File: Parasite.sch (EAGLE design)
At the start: 22 parts, among them U1 ATMEGA328PB-AU, U2 AD5262AD5262, U3 AD5262AD5262, U4 AD5262AD5262

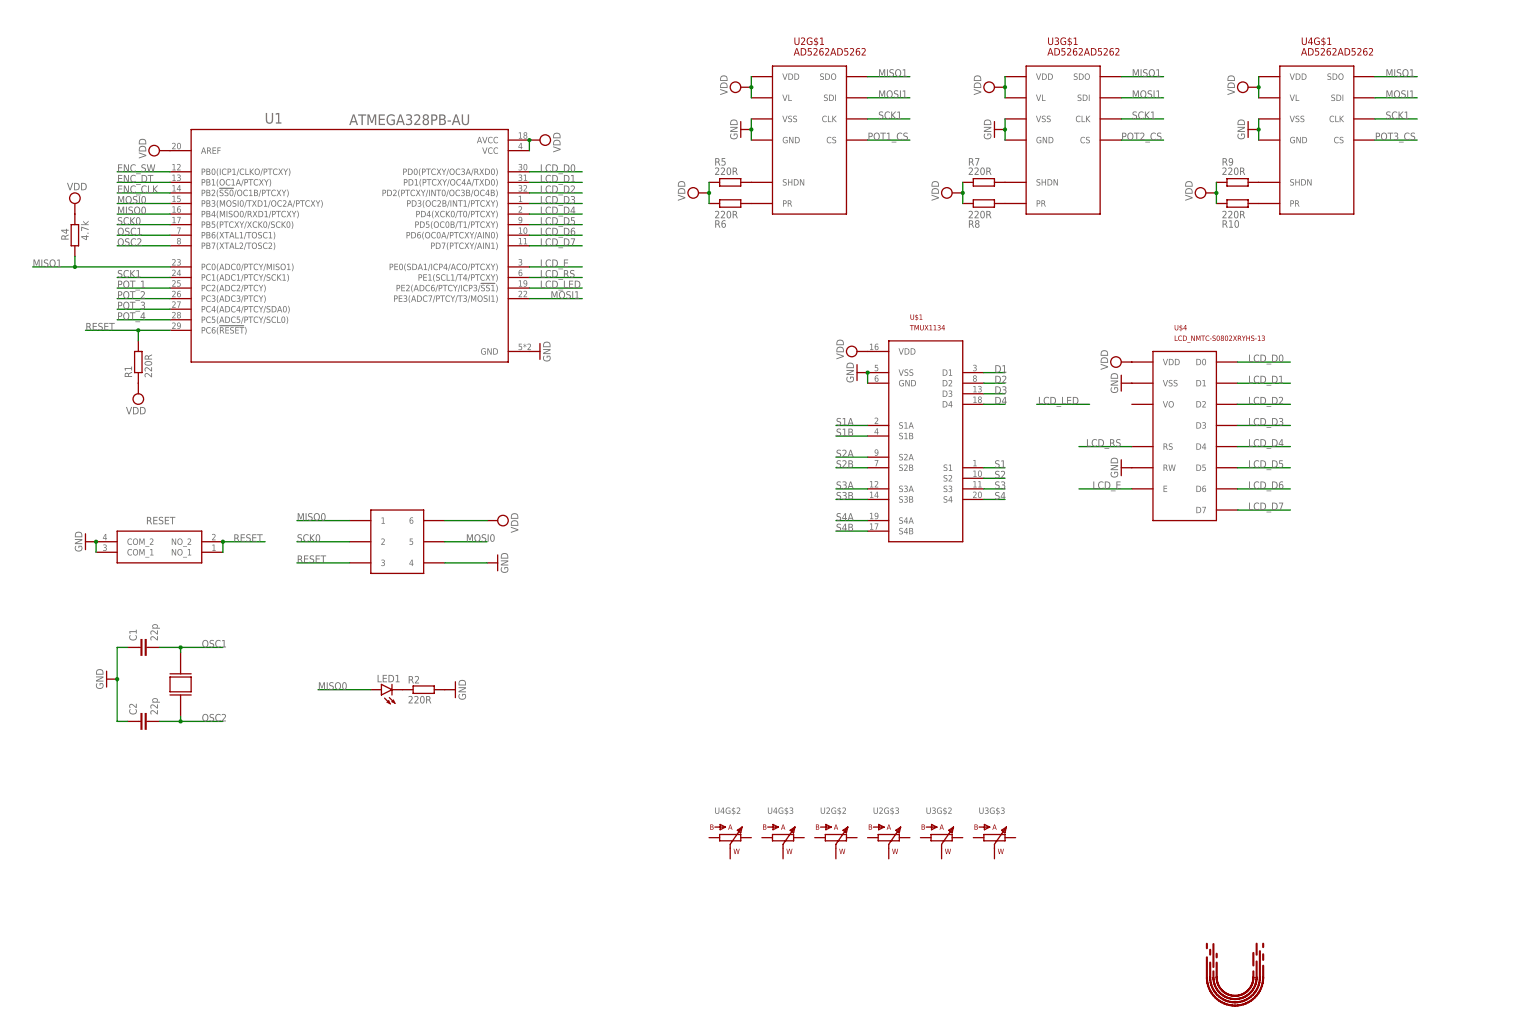
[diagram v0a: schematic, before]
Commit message: Added components and initialized layout
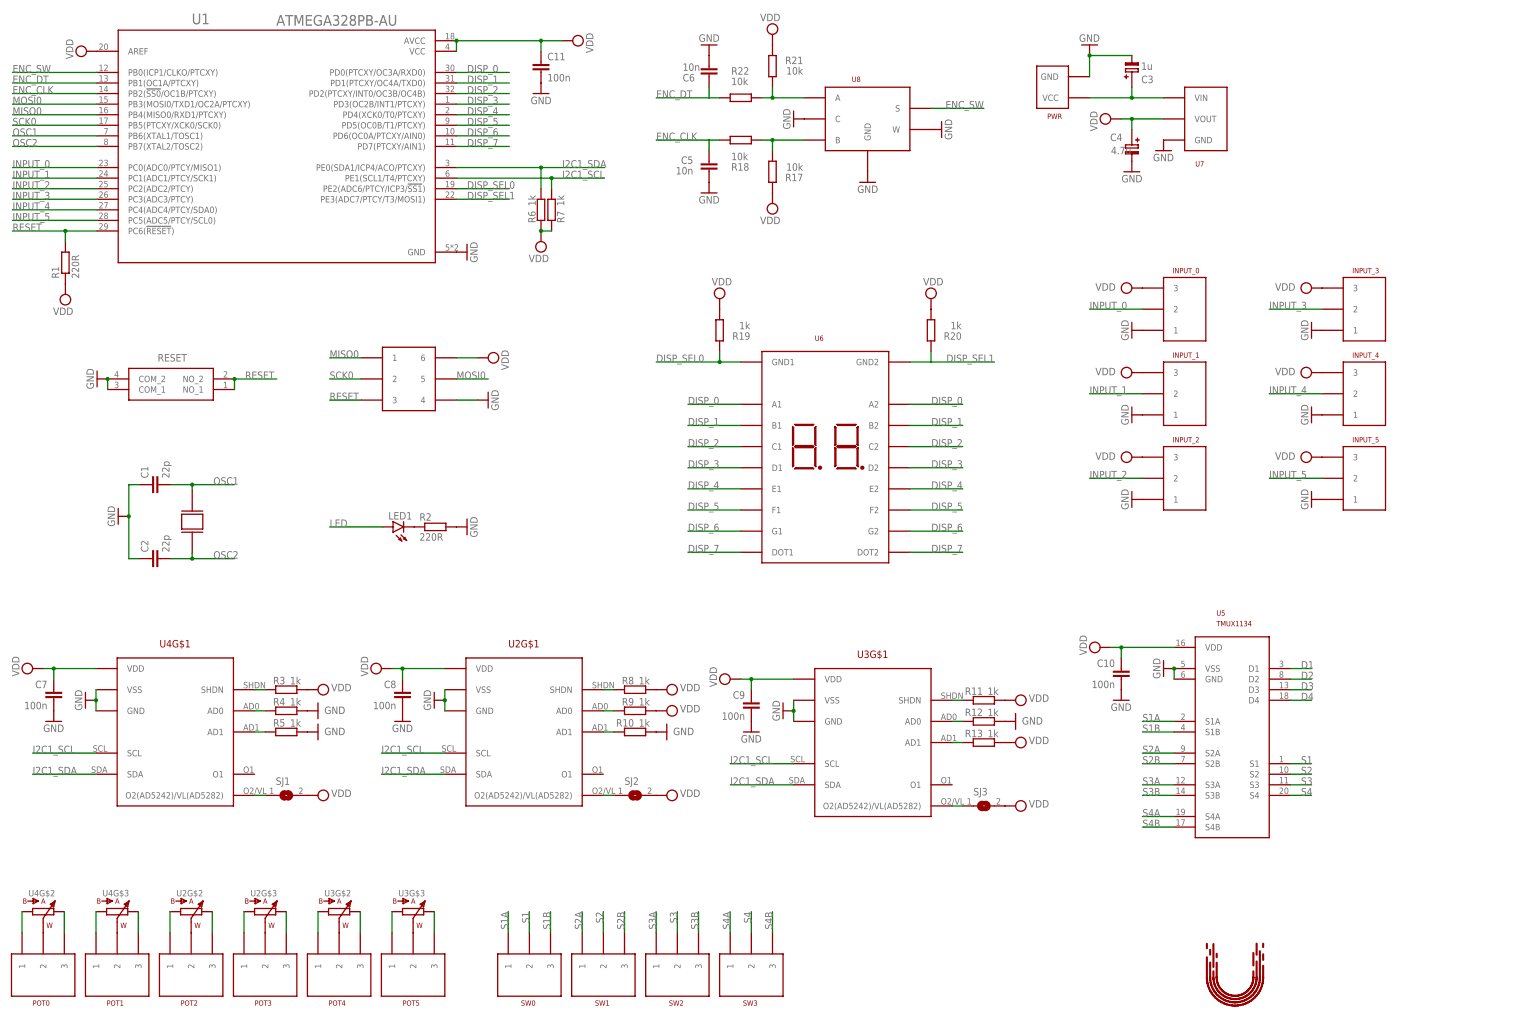
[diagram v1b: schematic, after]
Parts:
- removed U$1: TMUX1134, lib:TMUX1134
- removed U$4: LCD_NMTC-S0802XRYHS-13, lib:LCD_NMTC-S0802XRYHS-13
- added C10, C11, C7, C8, C9: 100n, lib:CAPACITOR1206
- added C3: 1u, lib:ELECT_CAPACITORCAP6
- added C4: 4.7u, lib:ELECT_CAPACITORCAP6
- added C5, C6: 10n, lib:CAPACITOR1206
- added INPUT_0, INPUT_1, INPUT_2, INPUT_3, INPUT_4, INPUT_5, POT0, POT1, POT2, POT3, POT4, POT5, SW0, SW1, SW2, SW3: 3_PIN_CONNECTOR, lib:3_PIN_CONNECTOR
- added PWR: PWR, lib:PWR
- added R11, R12, R13, R19, R20, R3: 1k, lib:RESISTOR1206
- added R17, R18, R21, R22: 10k, lib:RESISTOR1206
- added SJ1, SJ2, SJ3: (no value), lib:JUMPER
- added U5: TMUX1134, lib:TMUX1134
- added U6: 7_SEGMENT_DISPLAY, lib:7_SEGMENT_DISPLAY
- added U7: VOLTAGE_REGULATOR_LDL1117S50RVOLTAGE_REGULATOR_LDL1117S50R, lib:VOLTAGE_REGULATOR_LDL1117S50RVOLTAGE_REGULATOR_LDL1117S50R
- added U8: ROTARY_ENCODER, lib:ROTARY_ENCODER
- LED1: value LEDLED_1206 -> LEDLED_THROUGH; device lib:LEDLED_1206 -> lib:LEDLED_THROUGH
- R10, R5, R6, R7, R8, R9: value 220R -> 1k
- R4: value 4.7k -> 1k
- U2, U4: value AD5262AD5262 -> DIGITAL_POT_AD5242AD5242/AD5282; device lib:AD5262AD5262 -> lib:DIGITAL_POT_AD5242AD5242/AD5282
- U3: value AD5262AD5262 -> DIGITAL_POT_AD5282AD5242/AD5282; device lib:AD5262AD5262 -> lib:DIGITAL_POT_AD5282AD5242/AD5282
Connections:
- removed net LCD_D0: U$4.D0, U1.PD0(PTCXY/OC3A/RXD0)
- removed net LCD_D1: U$4.D1, U1.PD1(PTCXY/OC4A/TXD0)
- removed net LCD_D2: U$4.D2, U1.PD2(PTCXY/INT0/OC3B/OC4B)
- removed net LCD_D3: U$4.D3, U1.PD3(OC2B/INT1/PTCXY)
- removed net LCD_D4: U$4.D4, U1.PD4(XCK0/T0/PTCXY)
- removed net LCD_D5: U$4.D5, U1.PD5(OC0B/T1/PTCXY)
- removed net LCD_D6: U$4.D6, U1.PD6(OC0A/PTCXY/AIN0)
- removed net LCD_D7: U$4.D7, U1.PD7(PTCXY/AIN1)
- removed net LCD_E: U$4.E, U1.PE0(SDA1/ICP4/ACO/PTCXY)
- removed net LCD_LED: U1.PE2(ADC6/PTCY/ICP3/!SS1!)
- removed net LCD_RS: U$4.RS, U1.PE1(SCL1/T4/PTCXY)
- removed net MISO1: R4.1, U1.PC0(ADC0/PTCY/MISO1), U2G$1.SDO, U3G$1.SDO, U4G$1.SDO
- removed net MOSI1: U1.PE3(ADC7/PTCY/T3/MOSI1), U2G$1.SDI, U3G$1.SDI, U4G$1.SDI
- removed net POT1_CS: U2G$1.CS
- removed net POT2_CS: U3G$1.CS
- removed net POT3_CS: U4G$1.CS
- removed net POT_1: U1.PC2(ADC2/PTCY)
- removed net POT_2: U1.PC3(ADC3/PTCY)
- removed net POT_3: U1.PC4(ADC4/PTCY/SDA0)
- removed net POT_4: U1.PC5(ADC5/PTCY/SCL0)
- removed net SCK1: U1.PC1(ADC1/PTCY/SCK1), U2G$1.CLK, U3G$1.CLK, U4G$1.CLK
- new net DISP_0: U1.PD0(PTCXY/OC3A/RXD0), U6.A1, U6.A2
- new net DISP_1: U1.PD1(PTCXY/OC4A/TXD0), U6.B1, U6.B2
- new net DISP_2: U1.PD2(PTCXY/INT0/OC3B/OC4B), U6.C1, U6.C2
- new net DISP_3: U1.PD3(OC2B/INT1/PTCXY), U6.D1, U6.D2
- new net DISP_4: U1.PD4(XCK0/T0/PTCXY), U6.E1, U6.E2
- new net DISP_5: U1.PD5(OC0B/T1/PTCXY), U6.F1, U6.F2
- new net DISP_6: U1.PD6(OC0A/PTCXY/AIN0), U6.G1, U6.G2
- new net DISP_7: U1.PD7(PTCXY/AIN1), U6.DOT1, U6.DOT2
- new net DISP_SEL0: R19.1, U1.PE2(ADC6/PTCY/ICP3/!SS1!), U6.GND1
- new net DISP_SEL1: U1.PE3(ADC7/PTCY/T3/MOSI1), U6.GND2
- new net DISP_SEL2: R20.1
- new net I2C1_SCL: R7.1, U1.PE1(SCL1/T4/PTCXY), U2G$1.SCL, U3G$1.SCL, U4G$1.SCL
- new net I2C1_SDA: R6.1, U1.PE0(SDA1/ICP4/ACO/PTCXY), U2G$1.SDA, U3G$1.SDA, U4G$1.SDA
- new net INPUT_0: INPUT_0.2, U1.PC0(ADC0/PTCY/MISO1)
- new net INPUT_1: INPUT_1.2, U1.PC1(ADC1/PTCY/SCK1)
- new net INPUT_2: INPUT_2.2, U1.PC2(ADC2/PTCY)
- new net INPUT_3: INPUT_3.2, U1.PC3(ADC3/PTCY)
- new net INPUT_4: INPUT_4.2, U1.PC4(ADC4/PTCY/SDA0)
- new net INPUT_5: INPUT_5.2, U1.PC5(ADC5/PTCY/SCL0)
- new net LED: LED1.A
- new net N$10: SJ2.1, U2G$1.O2(AD5242)/VL(AD5282)
- new net N$11: R12.2, U3G$1.AD0
- new net N$12: R13.2, U3G$1.AD1
- new net N$13: SJ3.1, U3G$1.O2(AD5242)/VL(AD5282)
- new net N$18: POT0.2, U4G$2.W
- new net N$19: POT0.1, U4G$2.B
- new net N$2: R3.2, U4G$1.SHDN
- new net N$20: POT0.3, U4G$2.A
- new net N$21: POT1.1, U4G$3.B
- new net N$22: POT1.3, U4G$3.A
- new net N$23: POT1.2, U4G$3.W
- new net N$24: POT2.1, U2G$2.B
- new net N$25: POT2.3, U2G$2.A
- new net N$26: POT2.2, U2G$2.W
- new net N$27: POT3.1, U2G$3.B
- new net N$28: POT3.3, U2G$3.A
- new net N$29: POT3.2, U2G$3.W
- new net N$30: POT4.1, U3G$2.B
- new net N$31: POT4.3, U3G$2.A
- new net N$32: POT4.2, U3G$2.W
- new net N$33: POT5.1, U3G$3.B
- new net N$34: POT5.3, U3G$3.A
- new net N$35: POT5.2, U3G$3.W
- new net N$42: C3.+, PWR.VCC, U7.VIN
- new net N$43: R17.2, R18.1, U8.B
- new net N$45: R21.2, R22.1, U8.A
- new net N$9: R10.2, U2G$1.AD1
- net D1: now also U5.D1; no longer U$1.D1
- net D2: now also U5.D2; no longer U$1.D2
- net D3: now also U5.D3; no longer U$1.D3
- net D4: now also U5.D4; no longer U$1.D4
- net ENC_CLK: now also C5.2, R18.2
- net ENC_DT: now also C6.2, R22.2
- net ENC_SW: now also U8.S
- net GND: now also C10.2, C11.2, C3.-, C4.-, C5.1, C6.1, C7.2, C8.2, C9.2, INPUT_0.1, INPUT_1.1, INPUT_2.1, INPUT_3.1, INPUT_4.1, INPUT_5.1, PWR.GND, R10.1, R12.1, R4.1, R5.1, U5.GND, U5.VSS, U7.GND, U8.C, U8.GND, U8.W; no longer U$1.GND, U$1.VSS, U$4.RW, U$4.VSS
- net MISO0: no longer LED1.A
- net N$3: now also R4.2, U4G$1.AD0; no longer R5.2, U2G$1.SHDN
- net N$4: now also R5.2, U4G$1.AD1; no longer R6.2, U2G$1.PR
- net N$5: now also SJ1.1, U4G$1.O2(AD5242)/VL(AD5282); no longer R7.2, U3G$1.SHDN
- net N$6: now also R11.2, U3G$1.SHDN; no longer R8.2, U3G$1.PR
- net N$7: now also R8.2, U2G$1.SHDN; no longer R9.2, U4G$1.SHDN
- net N$8: now also R9.2, U2G$1.AD0; no longer R10.2, U4G$1.PR
- net S1: now also SW0.2, U5.S1; no longer U$1.S1
- net S1A: now also SW0.1, U5.S1A; no longer U$1.S1A
- net S1B: now also SW0.3, U5.S1B; no longer U$1.S1B
- net S2: now also SW1.2, U5.S2; no longer U$1.S2
- net S2A: now also SW1.1, U5.S2A; no longer U$1.S2A
- net S2B: now also SW1.3, U5.S2B; no longer U$1.S2B
- net S3: now also SW2.2, U5.S3; no longer U$1.S3
- net S3A: now also SW2.1, U5.S3A; no longer U$1.S3A
- net S3B: now also SW2.3, U5.S3B; no longer U$1.S3B
- net S4: now also SW3.2, U5.S4; no longer U$1.S4
- net S4A: now also SW3.1, U5.S4A; no longer U$1.S4A
- net S4B: now also SW3.3, U5.S4B; no longer U$1.S4B
- net VDD: now also C10.1, C11.1, C4.+, C7.1, C8.1, C9.1, INPUT_0.3, INPUT_1.3, INPUT_2.3, INPUT_3.3, INPUT_4.3, INPUT_5.3, R11.1, R13.1, R17.1, R19.2, R20.2, R21.1, R3.1, R6.2, R7.2, SJ1.2, SJ2.2, SJ3.2, U5.VDD, U7.VOUT; no longer R10.1, R4.2, R5.1, R6.1, R7.1, U$1.VDD, U$4.VDD, U2G$1.VL, U3G$1.VL, U4G$1.VL
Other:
- moved on the sheet: C1, C2, LED1, R1, R10, R2, R4, R5, R6, R7, R8, R9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

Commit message: Finished v1 layout
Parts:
- renumbered U$2 to U9, U$3 to U10
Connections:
- removed net DISP_SEL2: R20.1
- removed net LED: LED1.A
- removed net MOSI0: U1.PB3(MOSI0/TXD1/OC2A/PTCXY), U9.5
- removed net N$32: POT4.2, U3G$2.W
- removed net N$33: POT5.1, U3G$3.B
- removed net N$34: POT5.3, U3G$3.A
- removed net N$35: POT5.2, U3G$3.W
- new net MOSI0/LED: LED1.A, U1.PB3(MOSI0/TXD1/OC2A/PTCXY), U9.5
- new net N$14: POT2.2, U3G$3.W
- new net N$15: POT1.2, U2G$2.W
- new net N$16: POT0.2, U2G$3.W
- new net N$17: POT4.2, U4G$3.W
- net DISP_2: now also U6.E1, U6.E2; no longer U6.C1, U6.C2
- net DISP_4: now also U6.C1, U6.C2; no longer U6.E1, U6.E2
- net DISP_SEL1: now also R20.1
- net N$18: now also POT5.2; no longer POT0.2
- net N$19: now also POT3.2, U3G$2.W; no longer POT0.1, U4G$2.B
- net N$20: now also U2G$3.A; no longer U4G$2.A
- net N$21: now also POT0.1, U2G$3.B; no longer POT1.1, U4G$3.B
- net N$22: now also POT3.1, U3G$2.B; no longer POT1.3, U4G$3.A
- net N$23: now also POT3.3, U3G$2.A; no longer POT1.2, U4G$3.W
- net N$24: now also U3G$3.B; no longer U2G$2.B
- net N$25: now also U3G$3.A; no longer U2G$2.A
- net N$26: now also POT1.1, U2G$2.B; no longer POT2.2, U2G$2.W
- net N$27: now also POT1.3, U2G$2.A; no longer POT3.1, U2G$3.B
- net N$28: now also POT4.3, U4G$3.A; no longer POT3.3, U2G$3.A
- net N$29: now also POT5.3, U4G$2.A; no longer POT3.2, U2G$3.W
- net N$30: now also U4G$3.B; no longer U3G$2.B
- net N$31: now also POT5.1, U4G$2.B; no longer POT4.3, U3G$2.A
- net S1: now also SW1.2; no longer SW0.2
- net S1A: now also SW1.1; no longer SW0.1
- net S1B: now also SW1.3; no longer SW0.3
- net S2: now also SW0.2; no longer SW1.2
- net S2A: now also SW0.1; no longer SW1.1
- net S2B: now also SW0.3; no longer SW1.3
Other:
- moved on the sheet: SW0, SW1, SW2, SW3, U2G$2, U2G$3, U3G$2, U3G$3, U4G$2, U4G$3

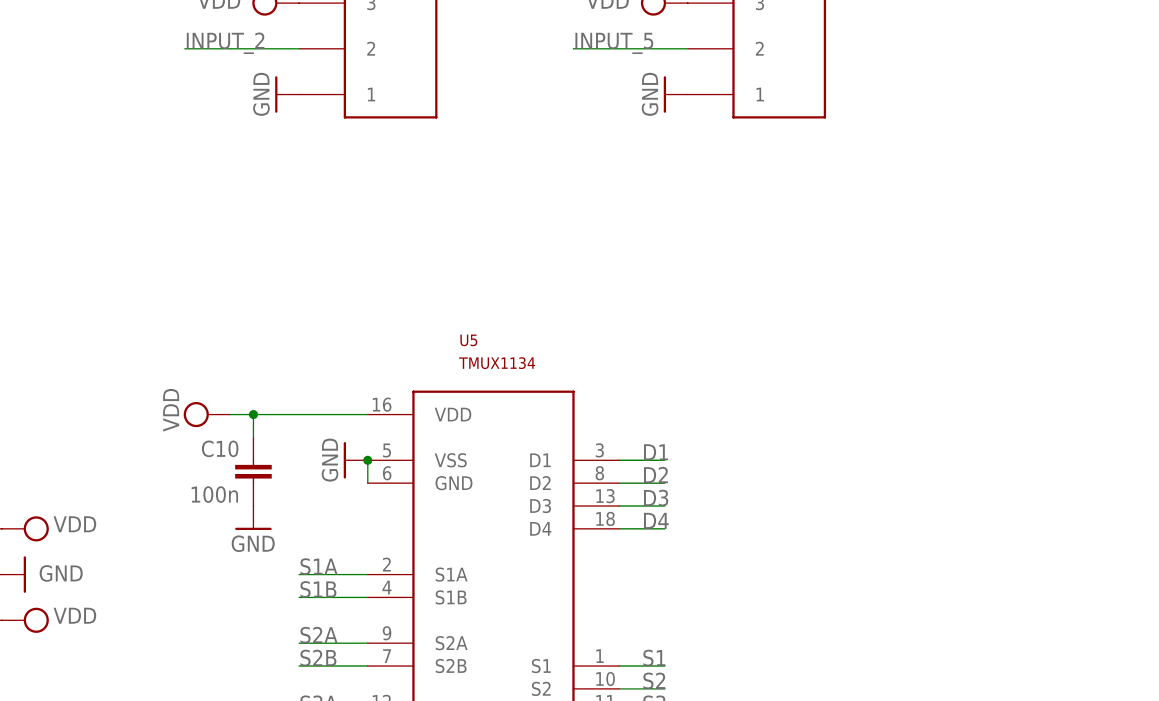
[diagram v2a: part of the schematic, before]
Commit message: Fixed encoder and restructure
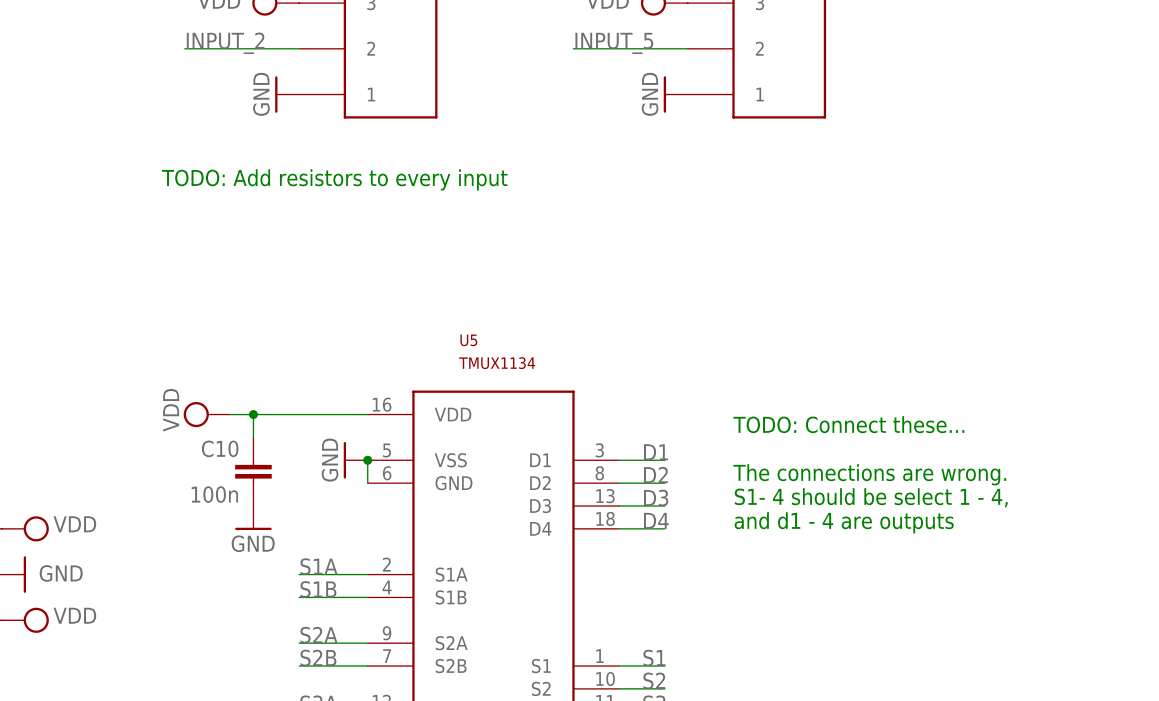
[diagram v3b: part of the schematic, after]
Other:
- note added: "TODO: Add resistors to every input"
- note added: "TODO: Connect these... The connections are wrong. S1- 4 should be select 1 - 4, and d1 - 4 are outputs"
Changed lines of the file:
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@@
 <sheet>
 <plain>
+<text x="340.36" y="81.28" size="1.778" layer="91">TODO: Connect these...
+The connections are wrong.
+S1- 4 should be select 1 - 4,
+and d1 - 4 are outputs</text>
+<text x="276.86" y="119.38" size="1.778" layer="91">TODO: Add resistors to every input</text>
 </plain>
 <instances>
@@
 </drawing>
 <compatibility>
+<note version="6.3" minversion="6.2.2" severity="warning">
+Since Version 6.2.2 text objects can contain more than one line,
+which will not be processed correctly with this version.
+</note>
 <note version="8.3" severity="warning">
 Since Version 8.3, EAGLE supports URNs for individual library
